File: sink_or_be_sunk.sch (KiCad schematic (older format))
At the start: 77 parts, among them J1 Grid_Conn_LED, J10 Grid_Conn, J11 Grid_Conn, J12 Grid_Conn, J13 Grid_Conn, J14 Grid_Conn, J15 Grid_Conn, J16 Grid_Conn, J18 Keypad_Conn, J19 Display_Conn, J2 Grid_Conn, J20 JTAG_Conn, J21 Debug_Conn, J22 Battery_Conn, J23 USB_B_Micro, J3 Grid_Conn, J4 Grid_Conn, J5 Grid_Conn, J6 Grid_Conn, J7 Grid_Conn, J8 Grid_Conn, J9 Grid_Conn, M1 Motor_DC, Q1 IRL530, Q2 Q_PMOS_GDS, Q3 2N3704, Q4 2N3704, SW1 SW_DPST, SW2 Reset_SW, U1 SN74HC151N, U2 SwitchingRegulator, U3 MCP73831-2-OT, U4 MCP608, U5 ESP32-WROOM-32, U6 CY7C65213A-28PVXI

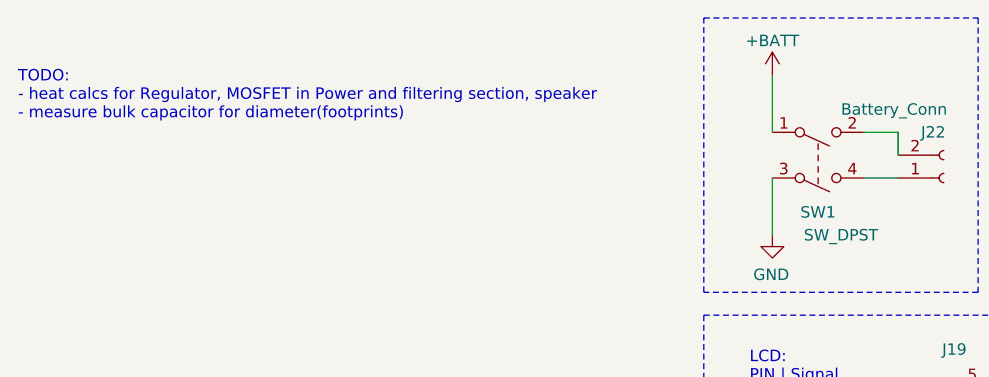
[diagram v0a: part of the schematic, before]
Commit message: added logo to board
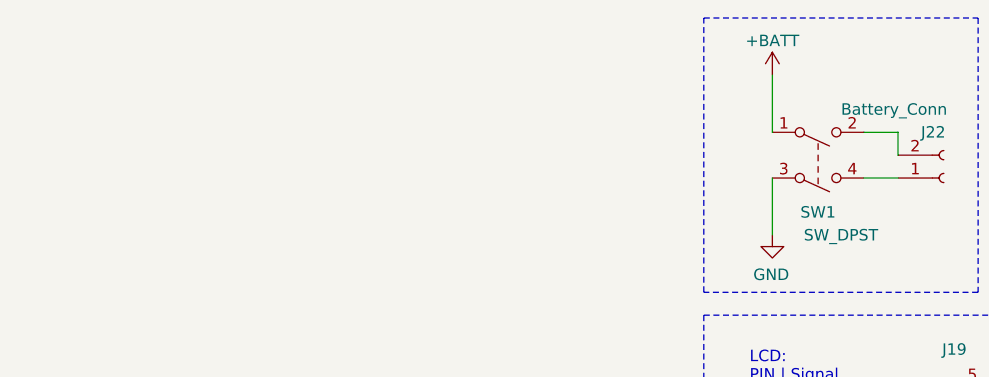
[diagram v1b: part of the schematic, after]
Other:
- note removed: "TODO: \n- heat calcs for Regulator, MOSFET in Power and filtering section, speaker\n- measure bulk capacitor for diameter(footprints)"
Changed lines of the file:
@@
 	1    0    0    -1
 $EndComp
-Text Notes -2450 1000 0    50   ~ 0
-TODO: \n- heat calcs for Regulator, MOSFET in Power and filtering section, speaker\n- measure bulk capacitor for diameter(footprints)
 Wire Wire Line
 	5050 4550 5050 5150

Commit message: added new connectors
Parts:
- J1: footprint Connector_JST:JST_EH_B7B-EH-A_1x07_P2.50mm_Vertical -> conn:TE_640456-7
- J10, J11, J12, J13, J14, J15, J16, J9, LS1, M1: footprint Connector_JST:JST_EH_B2B-EH-A_1x02_P2.50mm_Vertical -> conn:TE_640456-2
- J18: footprint Connector_JST:JST_EH_B8B-EH-A_1x08_P2.50mm_Vertical -> conn:TE_640456-8
- J19: footprint Connector_JST:JST_EH_B5B-EH-A_1x05_P2.50mm_Vertical -> conn:TE_640456-5
- J2, J3, J4, J5, J6, J7, J8: footprint Connector_JST:JST_EH_B6B-EH-A_1x06_P2.50mm_Vertical -> conn:TE_640456-6
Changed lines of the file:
@@
 F 0 "M1" V 2050 7450 50  0000 L CNN
 F 1 "Motor_DC" V 2150 7350 50  0000 L CNN
-F 2 "Connector_JST:JST_EH_B2B-EH-A_1x02_P2.50mm_Vertical" H 2350 7460 50  0001 C CNN
+F 2 "conn:TE_640456-2" H 2350 7460 50  0001 C CNN
 F 3 "~" H 2350 7460 50  0001 C CNN
 	1    2350 7550
@@
 F 0 "J19" H 1700 2000 50  0000 R CNN
 F 1 "Display_Conn" H 2400 2000 50  0000 R CNN
-F 2 "Connector_JST:JST_EH_B5B-EH-A_1x05_P2.50mm_Vertical" H 1600 2350 50  0001 C CNN
+F 2 "conn:TE_640456-5" H 1600 2350 50  0001 C CNN
 F 3 "~" H 1600 2350 50  0001 C CNN
 	1    1600 2350
@@
 F 0 "J18" H 800 3900 50  0000 R CNN
 F 1 "Keypad_Conn" H 1350 3900 50  0000 R CNN
-F 2 "Connector_JST:JST_EH_B8B-EH-A_1x08_P2.50mm_Vertical" H 700 3450 50  0001 C CNN
+F 2 "conn:TE_640456-8" H 700 3450 50  0001 C CNN
 F 3 "~" H 700 3450 50  0001 C CNN
 	1    700  3450
@@
 F 0 "LS1" H 5950 4450 50  0000 L CNN
 F 1 "Speaker" H 5900 4350 50  0000 L CNN
-F 2 "Connector_JST:JST_EH_B2B-EH-A_1x02_P2.50mm_Vertical" H 6050 4500 50  0001 C CNN
+F 2 "conn:TE_640456-2" H 6050 4500 50  0001 C CNN
 F 3 "~" H 6040 4650 50  0001 C CNN
 	1    6050 4700
@@
 F 0 "J2" H 9800 1450 50  0000 L CNN
 F 1 "Grid_Conn" H 9800 1350 50  0000 L CNN
-F 2 "Connector_JST:JST_EH_B6B-EH-A_1x06_P2.50mm_Vertical" H 10000 1050 50  0001 C CNN
+F 2 "conn:TE_640456-6" H 10000 1050 50  0001 C CNN
 F 3 "~" H 10000 1050 50  0001 C CNN
 	1    10000 1050
@@
 F 0 "J3" H 10300 1450 50  0000 L CNN
 F 1 "Grid_Conn" H 10300 1350 50  0000 L CNN
-F 2 "Connector_JST:JST_EH_B6B-EH-A_1x06_P2.50mm_Vertical" H 10500 1050 50  0001 C CNN
+F 2 "conn:TE_640456-6" H 10500 1050 50  0001 C CNN
 F 3 "~" H 10500 1050 50  0001 C CNN
 	1    10500 1050
@@
 F 0 "J7" H 10300 2450 50  0000 L CNN
 F 1 "Grid_Conn" H 10300 2350 50  0000 L CNN
-F 2 "Connector_JST:JST_EH_B6B-EH-A_1x06_P2.50mm_Vertical" H 10500 2050 50  0001 C CNN
+F 2 "conn:TE_640456-6" H 10500 2050 50  0001 C CNN
 F 3 "~" H 10500 2050 50  0001 C CNN
 	1    10500 2050
@@
 F 0 "J8" H 10800 2450 50  0000 L CNN
 F 1 "Grid_Conn" H 10800 2350 50  0000 L CNN
-F 2 "Connector_JST:JST_EH_B6B-EH-A_1x06_P2.50mm_Vertical" H 11000 2050 50  0001 C CNN
+F 2 "conn:TE_640456-6" H 11000 2050 50  0001 C CNN
 F 3 "~" H 11000 2050 50  0001 C CNN
 	1    11000 2050
@@
 F 0 "J5" H 9200 2450 50  0000 L CNN
 F 1 "Grid_Conn" H 9200 2350 50  0000 L CNN
-F 2 "Connector_JST:JST_EH_B6B-EH-A_1x06_P2.50mm_Vertical" H 9400 2050 50  0001 C CNN
+F 2 "conn:TE_640456-6" H 9400 2050 50  0001 C CNN
 F 3 "~" H 9400 2050 50  0001 C CNN
 	1    9400 2050
@@
 F 0 "J4" H 10800 1450 50  0000 L CNN
 F 1 "Grid_Conn" H 10800 1350 50  0000 L CNN
-F 2 "Connector_JST:JST_EH_B6B-EH-A_1x06_P2.50mm_Vertical" H 11000 1050 50  0001 C CNN
+F 2 "conn:TE_640456-6" H 11000 1050 50  0001 C CNN
 F 3 "~" H 11000 1050 50  0001 C CNN
 	1    11000 1050
@@
 F 0 "J6" H 9800 2450 50  0000 L CNN
 F 1 "Grid_Conn" H 9800 2350 50  0000 L CNN
-F 2 "Connector_JST:JST_EH_B6B-EH-A_1x06_P2.50mm_Vertical" H 10000 2050 50  0001 C CNN
+F 2 "conn:TE_640456-6" H 10000 2050 50  0001 C CNN
 F 3 "~" H 10000 2050 50  0001 C CNN
 	1    10000 2050
@@
 F 0 "J9" H 9100 3100 50  0000 L CNN
 F 1 "Grid_Conn" H 9100 3000 50  0000 L CNN
-F 2 "Connector_JST:JST_EH_B2B-EH-A_1x02_P2.50mm_Vertical" H 9300 2900 50  0001 C CNN
+F 2 "conn:TE_640456-2" H 9300 2900 50  0001 C CNN
 F 3 "~" H 9300 2900 50  0001 C CNN
 	1    9300 2900
@@
 F 0 "J10" H 9800 3100 50  0000 L CNN
 F 1 "Grid_Conn" H 9800 3000 50  0000 L CNN
-F 2 "Connector_JST:JST_EH_B2B-EH-A_1x02_P2.50mm_Vertical" H 10000 2900 50  0001 C CNN
+F 2 "conn:TE_640456-2" H 10000 2900 50  0001 C CNN
 F 3 "~" H 10000 2900 50  0001 C CNN
 	1    10000 2900
@@
 F 0 "J11" H 10300 3100 50  0000 L CNN
 F 1 "Grid_Conn" H 10300 3000 50  0000 L CNN
-F 2 "Connector_JST:JST_EH_B2B-EH-A_1x02_P2.50mm_Vertical" H 10500 2900 50  0001 C CNN
+F 2 "conn:TE_640456-2" H 10500 2900 50  0001 C CNN
 F 3 "~" H 10500 2900 50  0001 C CNN
 	1    10500 2900
@@
 F 0 "J12" H 10800 3100 50  0000 L CNN
 F 1 "Grid_Conn" H 10800 3000 50  0000 L CNN
-F 2 "Connector_JST:JST_EH_B2B-EH-A_1x02_P2.50mm_Vertical" H 11000 2900 50  0001 C CNN
+F 2 "conn:TE_640456-2" H 11000 2900 50  0001 C CNN
 F 3 "~" H 11000 2900 50  0001 C CNN
 	1    11000 2900
@@
 F 0 "J13" H 9100 3800 50  0000 L CNN
 F 1 "Grid_Conn" H 9100 3700 50  0000 L CNN
-F 2 "Connector_JST:JST_EH_B2B-EH-A_1x02_P2.50mm_Vertical" H 9300 3600 50  0001 C CNN
+F 2 "conn:TE_640456-2" H 9300 3600 50  0001 C CNN
 F 3 "~" H 9300 3600 50  0001 C CNN
 	1    9300 3600
@@
 F 0 "J14" H 9800 3800 50  0000 L CNN
 F 1 "Grid_Conn" H 9800 3700 50  0000 L CNN
-F 2 "Connector_JST:JST_EH_B2B-EH-A_1x02_P2.50mm_Vertical" H 10000 3600 50  0001 C CNN
+F 2 "conn:TE_640456-2" H 10000 3600 50  0001 C CNN
 F 3 "~" H 10000 3600 50  0001 C CNN
 	1    10000 3600
@@
 F 0 "J15" H 10300 3800 50  0000 L CNN
 F 1 "Grid_Conn" H 10300 3700 50  0000 L CNN
-F 2 "Connector_JST:JST_EH_B2B-EH-A_1x02_P2.50mm_Vertical" H 10500 3600 50  0001 C CNN
+F 2 "conn:TE_640456-2" H 10500 3600 50  0001 C CNN
 F 3 "~" H 10500 3600 50  0001 C CNN
 	1    10500 3600
@@
 F 0 "J16" H 10800 3800 50  0000 L CNN
 F 1 "Grid_Conn" H 10800 3700 50  0000 L CNN
-F 2 "Connector_JST:JST_EH_B2B-EH-A_1x02_P2.50mm_Vertical" H 11000 3600 50  0001 C CNN
+F 2 "conn:TE_640456-2" H 11000 3600 50  0001 C CNN
 F 3 "~" H 11000 3600 50  0001 C CNN
 	1    11000 3600
@@
 F 0 "J1" H 9050 1450 50  0000 L CNN
 F 1 "Grid_Conn_LED" H 9200 1450 50  0000 L CNN
-F 2 "Connector_JST:JST_EH_B7B-EH-A_1x07_P2.50mm_Vertical" H 9400 1050 50  0001 C CNN
+F 2 "conn:TE_640456-7" H 9400 1050 50  0001 C CNN
 F 3 "~" H 9400 1050 50  0001 C CNN
 	1    9400 1050

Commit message: cleaned up footprints
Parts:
- removed J23: USB_B_Micro, PCB_ESP32:USB_Micro_B_Female_Vert_1051330001, symbol sink_or_be_sunk-rescue:USB_B_Micro-Connector
- removed RV1: R_POT, PCB_ESP32:PinHeader_1x07_P2.54mm_Vertical, symbol grid:R_POT
- removed U1: SN74HC151N, Package_DIP:DIP-16_W10.16mm, symbol grid:SN74HC151N
- removed U2: SwitchingRegulator, PCB_ESP32:SwitchingRegulator, symbol grid:SwitchingRegulator
- removed U4: MCP608, Package_DIP:DIP-8_W7.62mm, symbol grid:MCP608
- added J17: USB_B_Micro, PCB_ESP32:USB_Micro_B_Female_Vert_1051330001, symbol Connector:USB_B_Micro
- added RV1: R_POT, Connector_PinHeader_2.54mm:PinHeader_1x07_P2.54mm_Vertical, symbol esp_board:R_POT
- added U1: SN74HC151N, Package_DIP:DIP-16_W10.16mm, symbol esp_board:SN74HC151N
- added U2: SwitchingRegulator, PCB_ESP32:SwitchingRegulator, symbol esp_board:SwitchingRegulator
- added U4: MCP608, Package_DIP:DIP-8_W7.62mm, symbol esp_board:MCP608
- J1: footprint conn:TE_640456-7 -> JST_Conn:TE_640456-7
- J10, J11, J12, J13, J14, J15, J16, J9: footprint conn:TE_640456-2 -> JST_Conn:TE_640456-2
- J2, J3, J4, J5, J6, J7, J8: footprint conn:TE_640456-6 -> JST_Conn:TE_640456-6
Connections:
- net +3V3: now also U1.8 (GND), U2.5 (Vout), U4.7
- net BOAT_INPUT: now also U1.13 (D6)
- net GND: now also J17.5 (GND), J17.6 (Shield), RV1.7, U1.15 (D4), U1.16 (VCC), U2.2 (On/Off), U2.3 (GND), U4.4, U4.8 (NCS)
- net MUX_R0: now also U1.12 (D7)
- net MUX_R1: now also U1.11 (A)
- net MUX_R2: now also U1.10 (B)
- net MUX_R3: now also U1.9 (C)
- net MUX_R4: now also U1.7 (~G)
- net MUX_R5: now also U1.6 (W)
- net MUX_R6: now also U1.5 (Y)
- net MUX_R7: now also U1.4 (D0)
- net MUX_ROW_SEL0: now also U1.3 (D1)
- net MUX_ROW_SEL1: now also U1.2 (D2)
- net MUX_ROW_SEL2: now also U1.1 (D3)
- net SPEAKER: now also U4.2
- net VBUS: now also J17.1 (VBUS)
- net Vin: now also U2.1 (Vin)
- net at U6.15 (USBDP): now also J17.3 (D+)
- net at U6.16 (USBDM): now also J17.2 (D-)
- net at C6.2: now also RV1.4
- net at RV2.1: now also U2.4 (Trim)
- new net: RV1.1, U4.3, U4.6
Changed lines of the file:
@@
-	1    0    0    -1
-$EndComp
-$Comp
-L grid:MCP608 U4
-U 1 1 6160D0C5
-P 4750 4550
-F 0 "U4" H 4900 4800 50  0000 L CNN
-F 1 "MCP608" H 4850 4700 50  0000 L CNN
-F 2 "Package_DIP:DIP-8_W7.62mm" H 4750 4550 50  0001 C CNN
-F 3 "https://www.microchip.com/content/dam/mchp/documents/APID/ProductDocuments/DataSheets/11177f.pdf" H 4750 4550 50  0001 C CNN
-	1    4750 4550
 	1    0    0    -1
 $EndComp
@@
 	-1   0    0    -1
 $EndComp
-$Comp
-L sink_or_be_sunk-rescue:USB_B_Micro-Connector J23
-U 1 1 61591780
-P 10000 4750
-F 0 "J23" H 10057 5217 50  0000 C CNN
-F 1 "USB_B_Micro" H 10057 5126 50  0000 C CNN
-F 2 "PCB_ESP32:USB_Micro_B_Female_Vert_1051330001" H 10150 4700 50  0001 C CNN
-F 3 "~" H 10150 4700 50  0001 C CNN
-	1    10000 4750
-	-1   0    0    -1
-$EndComp
 NoConn ~ 9500 4950
 Wire Wire Line
@@
 Wire Wire Line
 	850  6150 1700 6150
-$Comp
-L grid:SN74HC151N U?
-U 1 1 61628C20
-P 2000 6200
-AR Path="/6154E4DA/61628C20" Ref="U?"  Part="1"
-AR Path="/61628C20" Ref="U1"  Part="1"
-F 0 "U1" H 2000 5635 50  0000 C CNN
-F 1 "SN74HC151N" H 2000 5726 50  0000 C CNN
-F 2 "Package_DIP:DIP-16_W10.16mm" H 2050 6200 50  0001 C CNN
-F 3 "" H 2050 6200 50  0001 C CNN
-	1    2000 6200
-	-1   0    0    1
-$EndComp
 Wire Wire Line
 	950  3550 900  3550
@@
 Wire Wire Line
 	5050 4550 5400 4550
-Connection ~ 5050 4550
 Wire Wire Line
 	7250 6200 8050 6200
@@
 F 0 "J2" H 9800 1450 50  0000 L CNN
 F 1 "Grid_Conn" H 9800 1350 50  0000 L CNN
-F 2 "conn:TE_640456-6" H 10000 1050 50  0001 C CNN
+F 2 "JST_Conn:TE_640456-6" H 10000 1050 50  0001 C CNN
 F 3 "~" H 10000 1050 50  0001 C CNN
 	1    10000 1050
@@
 F 0 "J3" H 10300 1450 50  0000 L CNN
 F 1 "Grid_Conn" H 10300 1350 50  0000 L CNN
-F 2 "conn:TE_640456-6" H 10500 1050 50  0001 C CNN
+F 2 "JST_Conn:TE_640456-6" H 10500 1050 50  0001 C CNN
 F 3 "~" H 10500 1050 50  0001 C CNN
 	1    10500 1050
@@
 F 0 "J7" H 10300 2450 50  0000 L CNN
 F 1 "Grid_Conn" H 10300 2350 50  0000 L CNN
-F 2 "conn:TE_640456-6" H 10500 2050 50  0001 C CNN
+F 2 "JST_Conn:TE_640456-6" H 10500 2050 50  0001 C CNN
 F 3 "~" H 10500 2050 50  0001 C CNN
 	1    10500 2050
@@
 F 0 "J8" H 10800 2450 50  0000 L CNN
 F 1 "Grid_Conn" H 10800 2350 50  0000 L CNN
-F 2 "conn:TE_640456-6" H 11000 2050 50  0001 C CNN
+F 2 "JST_Conn:TE_640456-6" H 11000 2050 50  0001 C CNN
 F 3 "~" H 11000 2050 50  0001 C CNN
 	1    11000 2050
@@
 F 0 "J5" H 9200 2450 50  0000 L CNN
 F 1 "Grid_Conn" H 9200 2350 50  0000 L CNN
-F 2 "conn:TE_640456-6" H 9400 2050 50  0001 C CNN
+F 2 "JST_Conn:TE_640456-6" H 9400 2050 50  0001 C CNN
 F 3 "~" H 9400 2050 50  0001 C CNN
 	1    9400 2050
@@
 Connection ~ 9200 1050
 Connection ~ 9800 1050
-$Comp
-L grid:R_POT RV1
-U 1 1 64FDA131
-P 5400 4700
-F 0 "RV1" H 5331 4746 50  0000 R CNN
-F 1 "R_POT" H 5331 4655 50  0000 R CNN
-F 2 "PCB_ESP32:PinHeader_1x07_P2.54mm_Vertical" H 5400 4700 50  0001 C CNN
-F 3 "" H 5400 4700 50  0001 C CNN
-	1    5400 4700
-	1    0    0    -1
-$EndComp
 Text Label 8600 1250 0    50   ~ 0
 MUX_R0
@@
 F 0 "J4" H 10800 1450 50  0000 L CNN
 F 1 "Grid_Conn" H 10800 1350 50  0000 L CNN
-F 2 "conn:TE_640456-6" H 11000 1050 50  0001 C CNN
+F 2 "JST_Conn:TE_640456-6" H 11000 1050 50  0001 C CNN
 F 3 "~" H 11000 1050 50  0001 C CNN
 	1    11000 1050
@@
 F 0 "J6" H 9800 2450 50  0000 L CNN
 F 1 "Grid_Conn" H 9800 2350 50  0000 L CNN
-F 2 "conn:TE_640456-6" H 10000 2050 50  0001 C CNN
+F 2 "JST_Conn:TE_640456-6" H 10000 2050 50  0001 C CNN
 F 3 "~" H 10000 2050 50  0001 C CNN
 	1    10000 2050
@@
 F 0 "J9" H 9100 3100 50  0000 L CNN
 F 1 "Grid_Conn" H 9100 3000 50  0000 L CNN
-F 2 "conn:TE_640456-2" H 9300 2900 50  0001 C CNN
+F 2 "JST_Conn:TE_640456-2" H 9300 2900 50  0001 C CNN
 F 3 "~" H 9300 2900 50  0001 C CNN
 	1    9300 2900
@@
 F 0 "J10" H 9800 3100 50  0000 L CNN
 F 1 "Grid_Conn" H 9800 3000 50  0000 L CNN
-F 2 "conn:TE_640456-2" H 10000 2900 50  0001 C CNN
+F 2 "JST_Conn:TE_640456-2" H 10000 2900 50  0001 C CNN
 F 3 "~" H 10000 2900 50  0001 C CNN
 	1    10000 2900
@@
 F 0 "J11" H 10300 3100 50  0000 L CNN
 F 1 "Grid_Conn" H 10300 3000 50  0000 L CNN
-F 2 "conn:TE_640456-2" H 10500 2900 50  0001 C CNN
+F 2 "JST_Conn:TE_640456-2" H 10500 2900 50  0001 C CNN
 F 3 "~" H 10500 2900 50  0001 C CNN
 	1    10500 2900
@@
 F 0 "J12" H 10800 3100 50  0000 L CNN
 F 1 "Grid_Conn" H 10800 3000 50  0000 L CNN
-F 2 "conn:TE_640456-2" H 11000 2900 50  0001 C CNN
+F 2 "JST_Conn:TE_640456-2" H 11000 2900 50  0001 C CNN
 F 3 "~" H 11000 2900 50  0001 C CNN
 	1    11000 2900
@@
 F 0 "J13" H 9100 3800 50  0000 L CNN
 F 1 "Grid_Conn" H 9100 3700 50  0000 L CNN
-F 2 "conn:TE_640456-2" H 9300 3600 50  0001 C CNN
+F 2 "JST_Conn:TE_640456-2" H 9300 3600 50  0001 C CNN
 F 3 "~" H 9300 3600 50  0001 C CNN
 	1    9300 3600
@@
 F 0 "J14" H 9800 3800 50  0000 L CNN
 F 1 "Grid_Conn" H 9800 3700 50  0000 L CNN
-F 2 "conn:TE_640456-2" H 10000 3600 50  0001 C CNN
+F 2 "JST_Conn:TE_640456-2" H 10000 3600 50  0001 C CNN
 F 3 "~" H 10000 3600 50  0001 C CNN
 	1    10000 3600
@@
 F 0 "J15" H 10300 3800 50  0000 L CNN
 F 1 "Grid_Conn" H 10300 3700 50  0000 L CNN
-F 2 "conn:TE_640456-2" H 10500 3600 50  0001 C CNN
+F 2 "JST_Conn:TE_640456-2" H 10500 3600 50  0001 C CNN
 F 3 "~" H 10500 3600 50  0001 C CNN
 	1    10500 3600
@@
 F 0 "J16" H 10800 3800 50  0000 L CNN
 F 1 "Grid_Conn" H 10800 3700 50  0000 L CNN
-F 2 "conn:TE_640456-2" H 11000 3600 50  0001 C CNN
+F 2 "JST_Conn:TE_640456-2" H 11000 3600 50  0001 C CNN
 F 3 "~" H 11000 3600 50  0001 C CNN
 	1    11000 3600
@@
 F 0 "J1" H 9050 1450 50  0000 L CNN
 F 1 "Grid_Conn_LED" H 9200 1450 50  0000 L CNN
-F 2 "conn:TE_640456-7" H 9400 1050 50  0001 C CNN
+F 2 "JST_Conn:TE_640456-7" H 9400 1050 50  0001 C CNN
 F 3 "~" H 9400 1050 50  0001 C CNN
 	1    9400 1050
@@
 	1750 4550 1750 4700
 $Comp
-L grid:SwitchingRegulator U2
-U 1 1 6198BEB8
+L Connector:USB_B_Micro J17
+U 1 1 619C22A6
+P 10000 4750
+F 0 "J17" H 9770 4739 50  0000 R CNN
+F 1 "USB_B_Micro" H 9770 4648 50  0000 R CNN
+F 2 "PCB_ESP32:USB_Micro_B_Female_Vert_1051330001" H 10150 4700 50  0001 C CNN
+F 3 "~" H 10150 4700 50  0001 C CNN
+	1    10000 4750
+	-1   0    0    -1
+$EndComp
+$Comp
+L esp_board:R_POT RV1
+U 1 1 619E3CEA
+P 5400 4700
+F 0 "RV1" H 5300 4650 50  0000 R CNN
+F 1 "R_POT" H 5300 4550 50  0000 R CNN
+F 2 "Connector_PinHeader_2.54mm:PinHeader_1x07_P2.54mm_Vertical" H 5400 4700 50  0001 C CNN
+F 3 "" H 5400 4700 50  0001 C CNN
+	1    5400 4700
+	1    0    0    -1
+$EndComp
+$Comp
+L esp_board:MCP608 U4
+U 1 1 619E4E71
+P 4750 4550
+F 0 "U4" H 5000 4650 50  0000 L CNN
+F 1 "MCP608" H 5150 4650 50  0000 L CNN
+F 2 "Package_DIP:DIP-8_W7.62mm" H 4750 4550 50  0001 C CNN
+F 3 "" H 4750 4550 50  0001 C CNN
+	1    4750 4550
+	1    0    0    -1
+$EndComp
+Connection ~ 5050 4550
+$Comp
+L esp_board:SN74HC151N U1
+U 1 1 61A04FB0
+P 2000 6200
+F 0 "U1" H 2000 6775 50  0000 C CNN
+F 1 "SN74HC151N" H 2000 6684 50  0000 C CNN
+F 2 "Package_DIP:DIP-16_W10.16mm" H 2050 6200 50  0001 C CNN
+F 3 "" H 2050 6200 50  0001 C CNN
+	1    2000 6200
+	1    0    0    -1
+$EndComp
+$Comp
+L esp_board:SwitchingRegulator U2
+U 1 1 61A086E5
 P 2400 4800
 F 0 "U2" H 2350 5315 50  0000 C CNN
 F 1 "SwitchingRegulator" H 2350 5224 50  0000 C CNN
 F 2 "PCB_ESP32:SwitchingRegulator" H 2400 4800 50  0001 C CNN
-F 3 "https://www.mouser.com/datasheet/2/632/dele_s_a0000496181_1-2289578.pdf" H 2400 4800 50  0001 C CNN
+F 3 "" H 2400 4800 50  0001 C CNN
 	1    2400 4800
 	1    0    0    -1

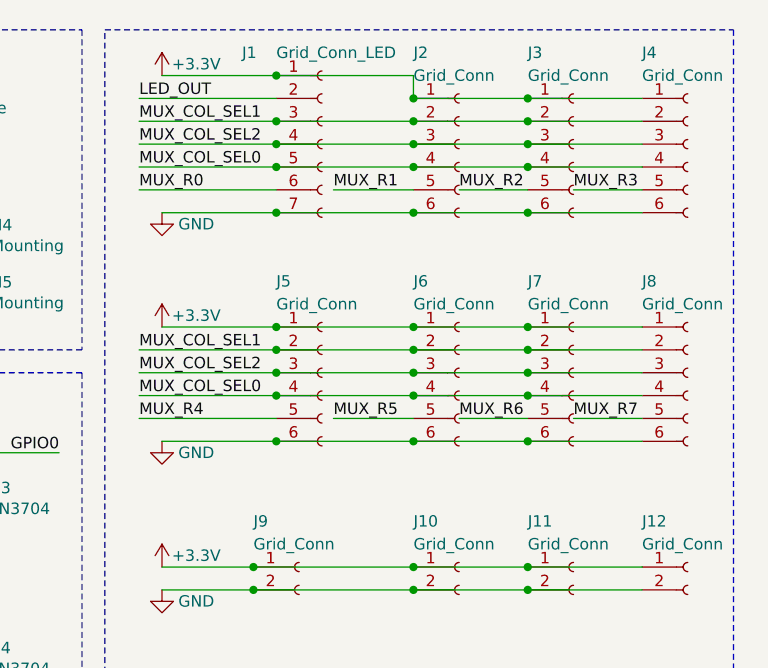
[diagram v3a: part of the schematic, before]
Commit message: updated library with footprints
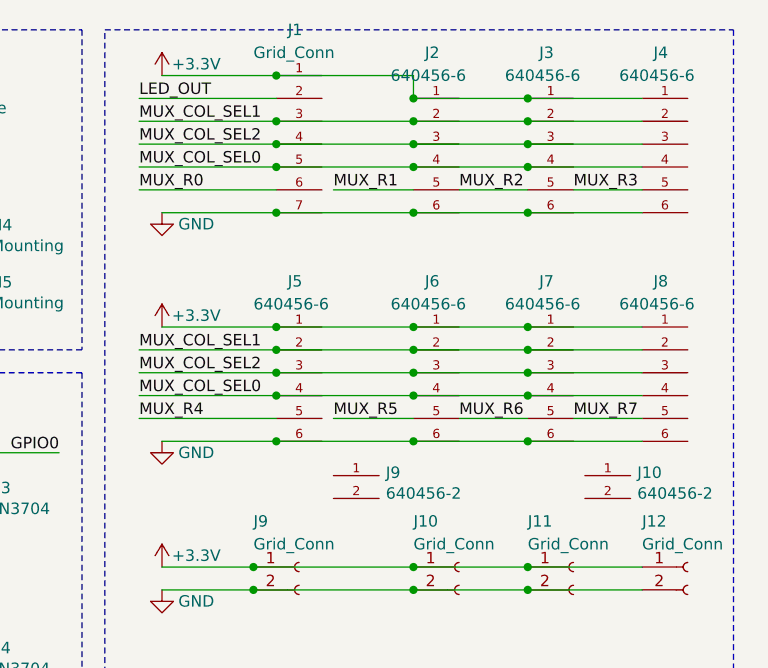
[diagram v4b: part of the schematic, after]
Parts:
- removed J1: Grid_Conn_LED, JST_Conn:TE_640456-7, symbol Connector:Conn_01x07_Female
- removed J2, J3, J4, J5, J6, J7, J8: Grid_Conn, JST_Conn:TE_640456-6, symbol Connector:Conn_01x06_Female
- added J1: Grid_Conn, JST_Conn:TE_640456-7, symbol JST_Conn:640456-7
- added J10, J9: 640456-2, JST_Conn:TE_640456-2, symbol JST_Conn:640456-2
- added J2, J3, J4, J5, J6, J7, J8: 640456-6, JST_Conn:TE_640456-6, symbol JST_Conn:640456-6
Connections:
- net +3V3: now also J1.1, J2.1, J3.1, J4.1, J5.1, J6.1, J7.1, J8.1
- net GND: now also J1.7, J2.6, J3.6, J4.6, J5.6, J6.6, J7.6, J8.6
- net LED_OUT: now also J1.2
- net MUX_COL_SEL0: now also J1.5, J2.4, J3.4, J4.4, J5.4, J6.4, J7.4, J8.4
- net MUX_COL_SEL1: now also J1.3, J2.2, J3.2, J4.2, J5.2, J6.2, J7.2, J8.2
- net MUX_COL_SEL2: now also J1.4, J2.3, J3.3, J4.3, J5.3, J6.3, J7.3, J8.3
- net MUX_R0: now also J1.6
- net MUX_R1: now also J2.5
- net MUX_R2: now also J3.5
- net MUX_R3: now also J4.5
- net MUX_R4: now also J5.5
- net MUX_R5: now also J6.5
- net MUX_R6: now also J7.5
- net MUX_R7: now also J8.5
